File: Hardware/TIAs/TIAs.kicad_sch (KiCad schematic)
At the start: 13 parts, among them U1 MCP6L01x-xOT, U5 MCP6L01x-xOT

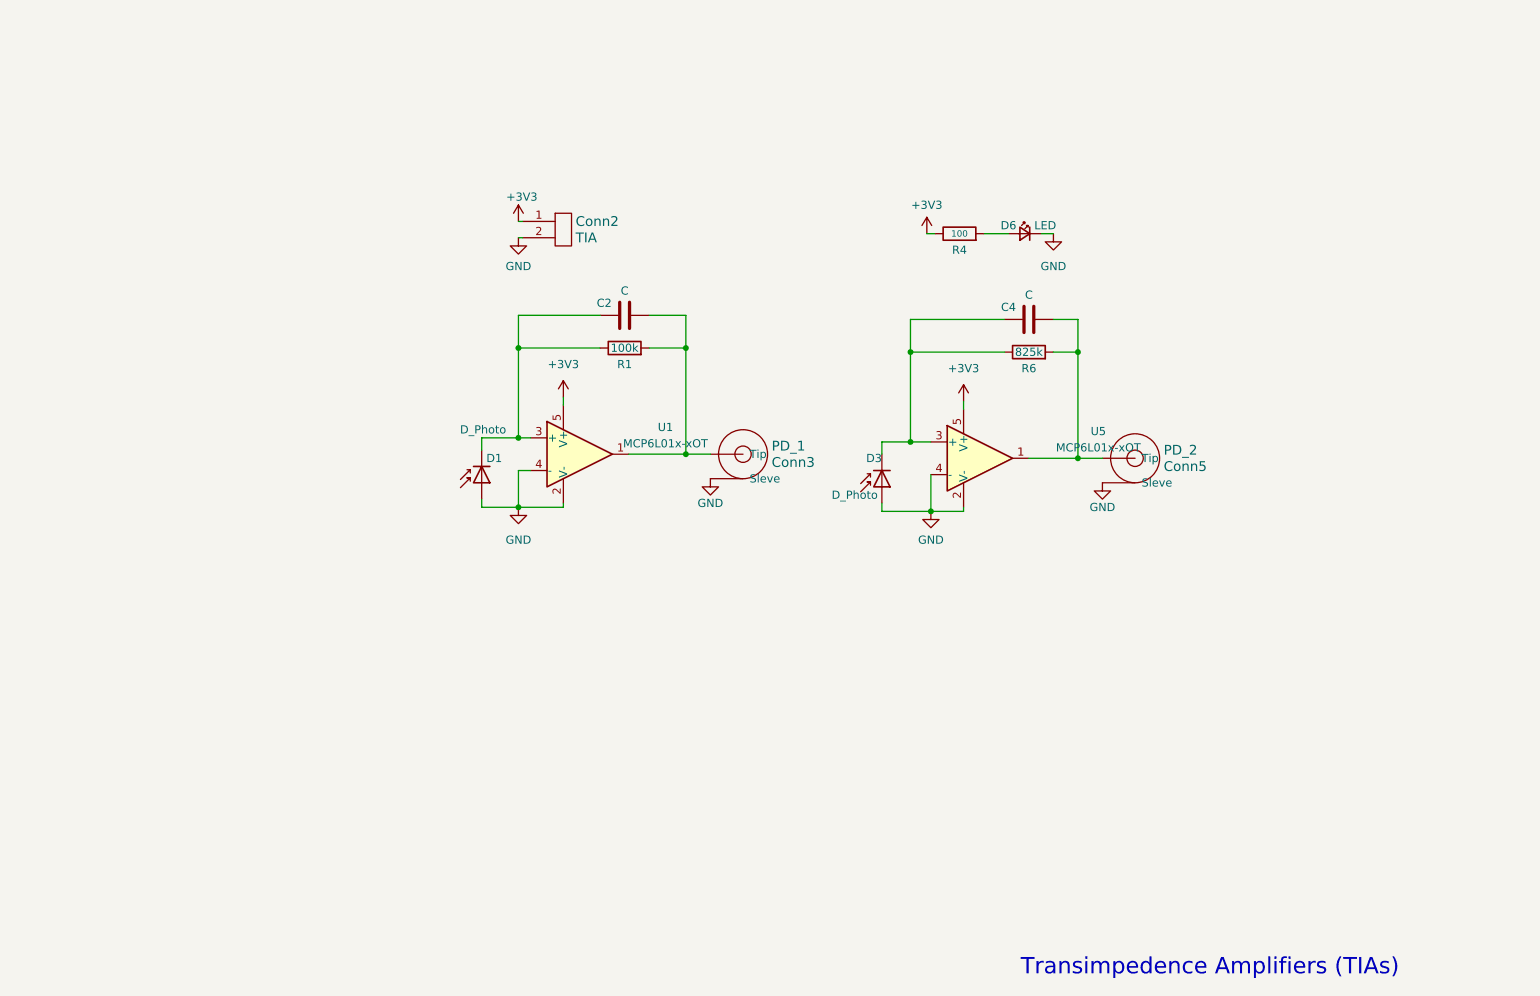
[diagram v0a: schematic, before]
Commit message: Footprint assignments
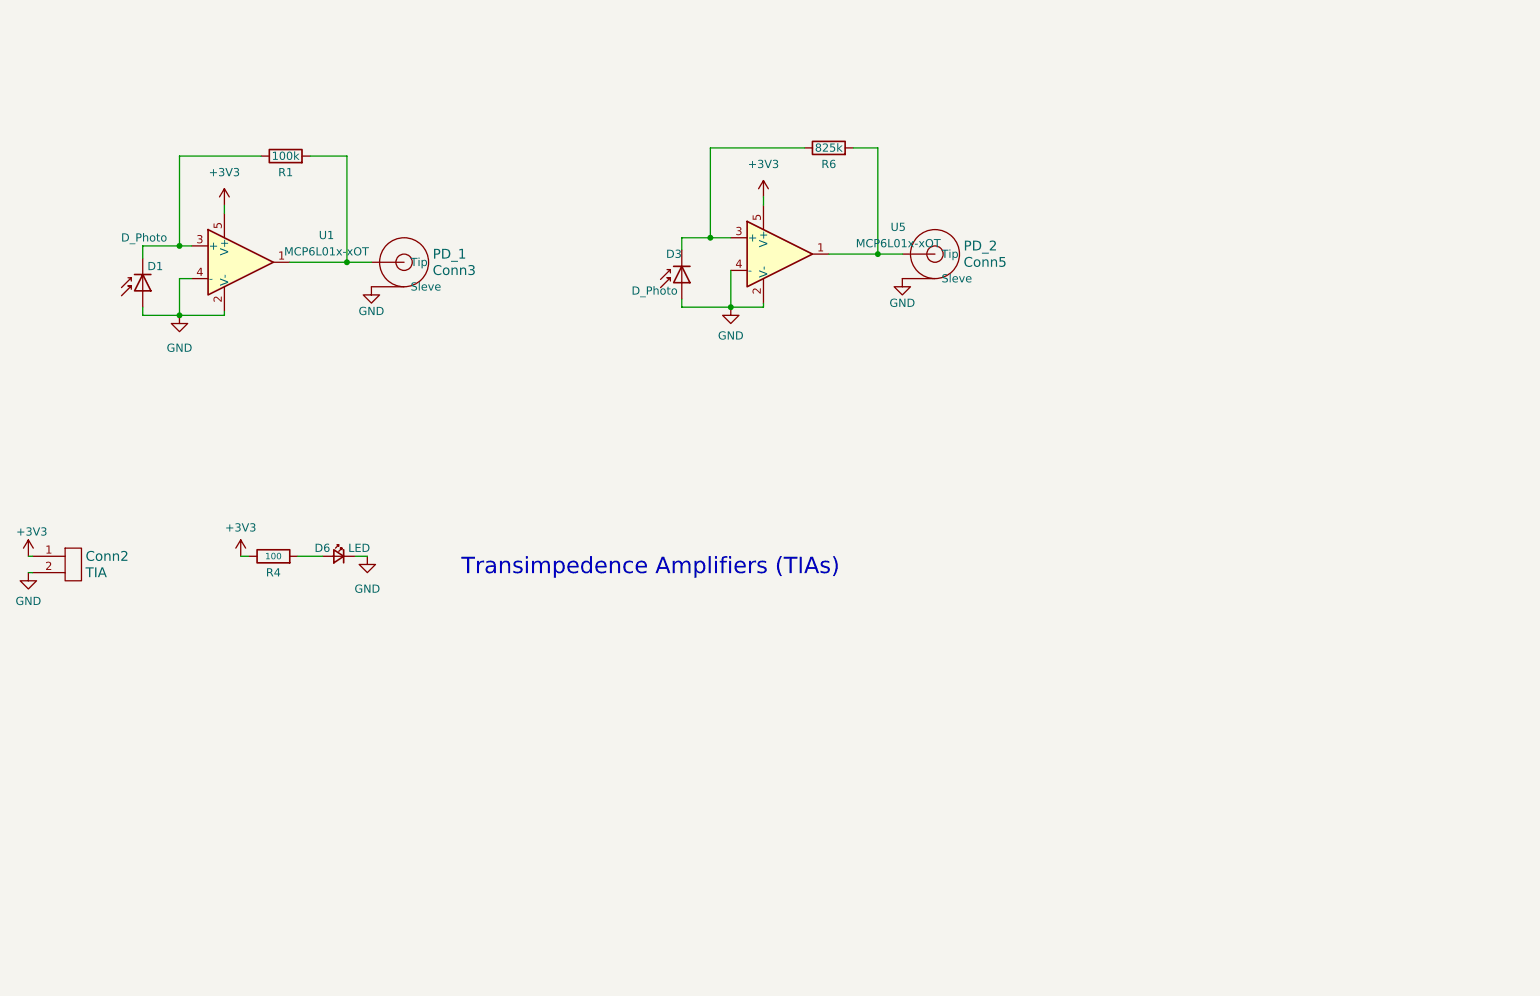
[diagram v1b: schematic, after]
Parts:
- removed C2, C4: C, symbol Device:C
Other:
- moved on the sheet: Conn2, Conn3, Conn5, D1, D3, D6, R1, R4, R6, U1, U5

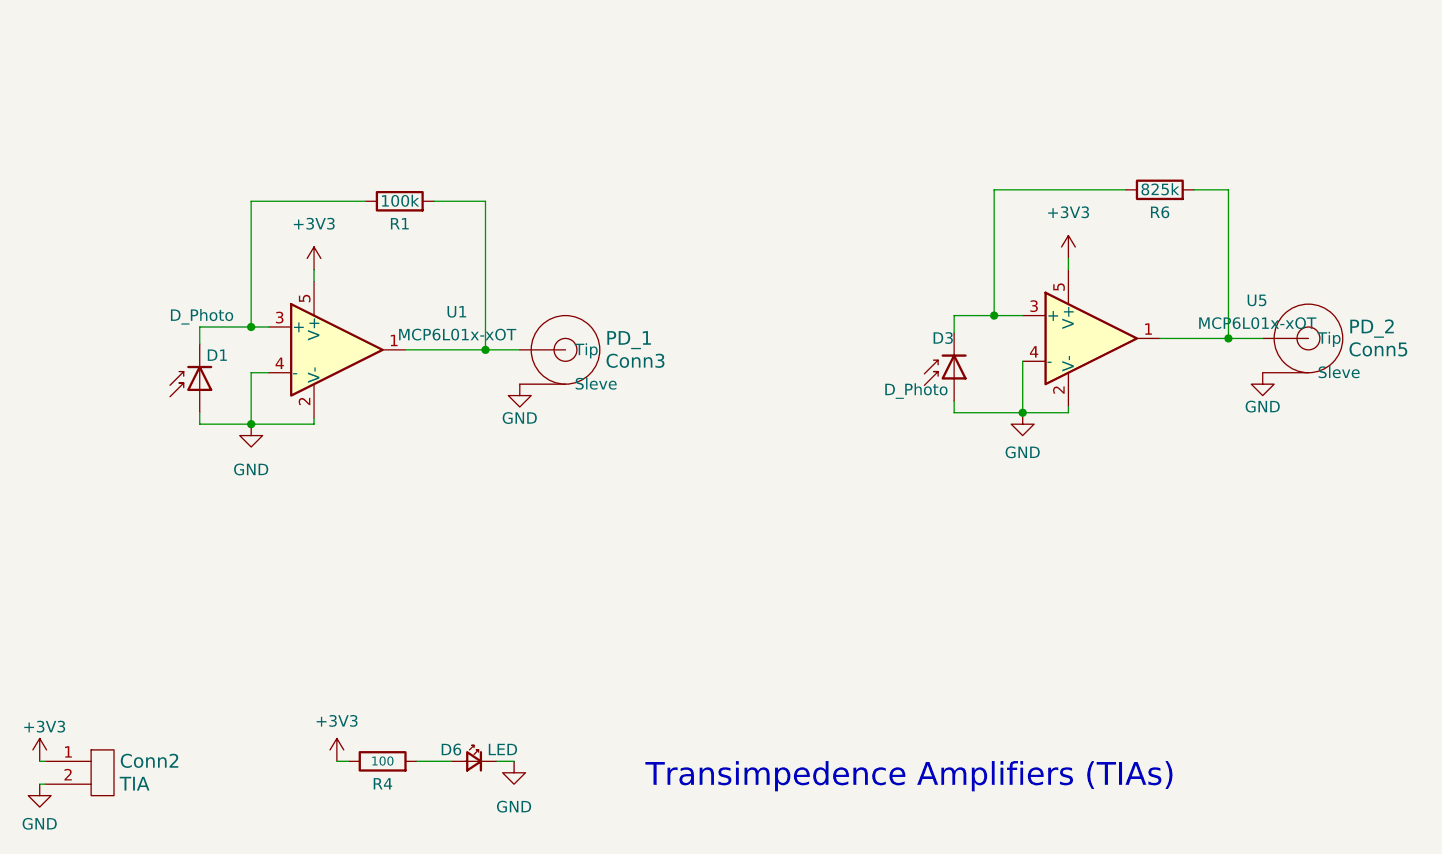
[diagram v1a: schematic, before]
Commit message: Separated Layouts
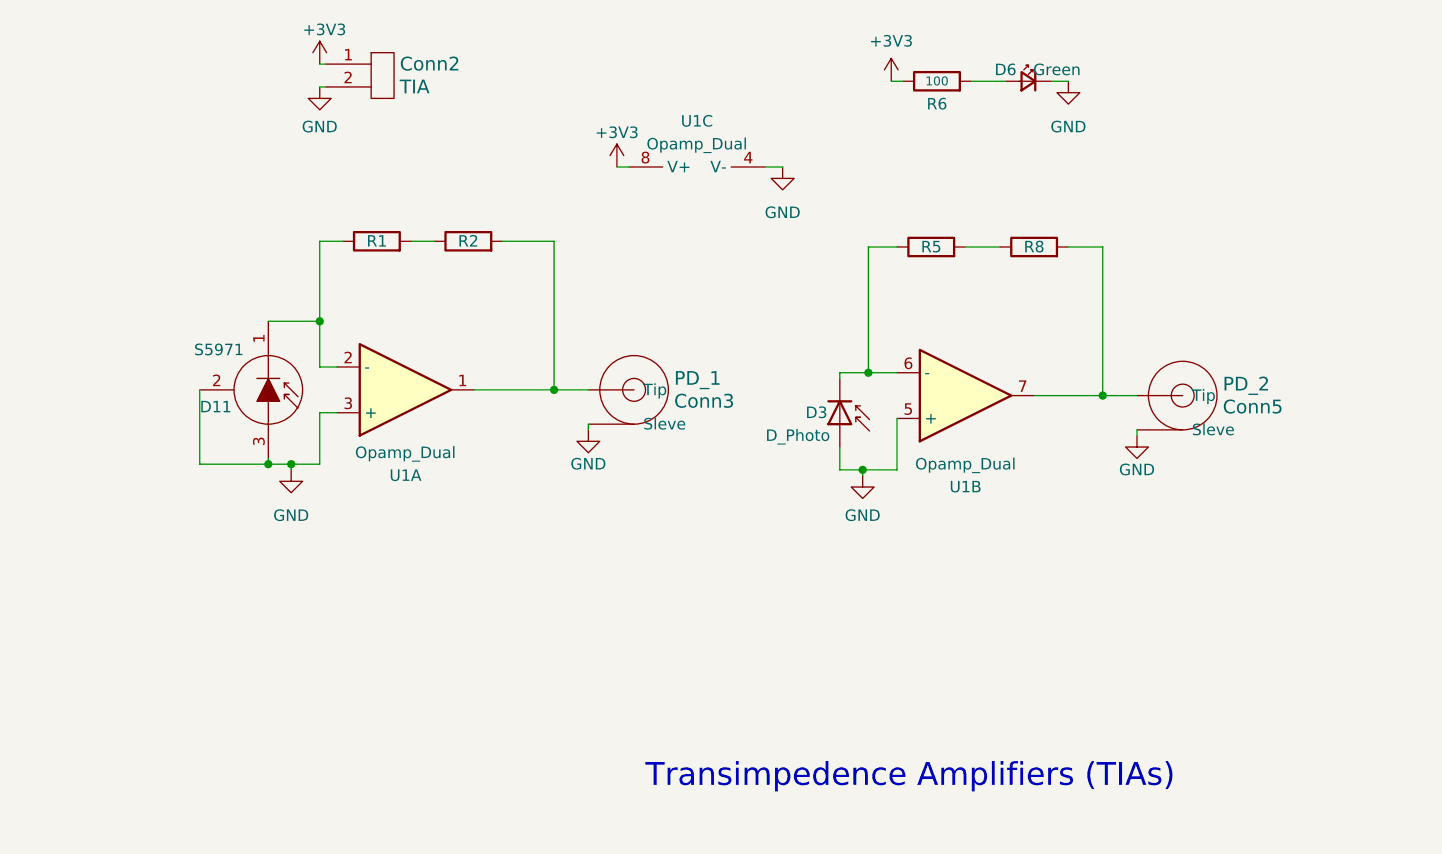
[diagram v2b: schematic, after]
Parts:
- removed D1: D_Photo, symbol Device:D_Photo
- removed R4: 100, Resistor_SMD:R_0603_1608Metric_Pad0.98x0.95mm_HandSolder, symbol Device:R
- removed U1, U5: MCP6L01x-xOT, Package_TO_SOT_SMD:SOT-23-5, symbol Amplifier_Operational:MCP6L01x-xOT
- added D11: S5971, FTIR_Footprints:P16113-011MN, symbol Sensor_Optical:S5971
- added R2, R5, R8: ~, LED_SMD:LED_0603_1608Metric_Pad1.05x0.95mm_HandSolder, symbol Device:R
- added U1: Opamp_Dual, Package_SO:SO-8_3.9x4.9mm_P1.27mm, symbol Device:Opamp_Dual
- Conn2: footprint (none) -> MRDT_Connectors:MOLEX_SL_02_Vertical
- Conn3, Conn5: footprint (none) -> FTIR_Footprints:142-0701-801
- D3: footprint (none) -> FTIR_Footprints:VTP9812FH
- D6: value LED -> Green
- R1: value 100k -> ~; footprint (none) -> LED_SMD:LED_0603_1608Metric_Pad1.05x0.95mm_HandSolder
- R6: value 825k -> 100; footprint (none) -> Resistor_SMD:R_0603_1608Metric_Pad0.98x0.95mm_HandSolder
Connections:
- net +3V3: now also R6.1, U1.8 (V+)
- net GND: now also D11.2 (C), D11.3 (A), U1.3 (+), U1.4 (V-), U1.5 (+)
- net at D3.1 (K): now also R5.1, U1.6 (-); no longer R6.1
- net at R1.1: now also D11.1 (K), U1.2 (-)
- net at Conn3.1 (Tip): now also R2.2, U1.1; no longer R1.2
- net at Conn5.1 (Tip): now also R8.2, U1.7; no longer R6.2
- net at D6.2 (A): now also R6.2
- new net: R1.2, R2.1
- new net: R5.2, R8.1

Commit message: Moved breakout boards to separate layouts
Edge cut no work :,(
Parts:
- added H1, H2, H3, H4: MountingHole, MRDT_Drill_Holes:4_40_Hole_Corner, symbol Mechanical:MountingHole
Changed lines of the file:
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@@
+    )
+  )
+  (symbol (lib_id "Mechanical:MountingHole") (at 160.02 39.37 0) (unit 1)
+    (in_bom yes) (on_board yes) (dnp no) (fields_autoplaced)
+    (property "Reference" "H2" (at 163.195 38.0999 0)
+      (effects (font (size 1.27 1.27)) (justify left))
+    )
+    (property "Value" "MountingHole" (at 163.195 40.6399 0)
+      (effects (font (size 1.27 1.27)) (justify left))
+    )
+    (property "Footprint" "MRDT_Drill_Holes:4_40_Hole_Corner" (at 160.02 39.37 0)
+      (effects (font (size 1.27 1.27)) hide)
+    )
+    (property "Datasheet" "~" (at 160.02 39.37 0)
+      (effects (font (size 1.27 1.27)) hide)
+    )
+    (instances
+      (project "FTIR_Main_Hardware"
+        (path "/049c3f09-c046-40c3-9872-e62b40667976"
+          (reference "H2") (unit 1)
+        )
+      )
+      (project "Flouro_Breakout"
+        (path "/7d297d96-3ae7-4136-8d04-aa7759bb4b4b"
+          (reference "H2") (unit 1)
+        )
+      )
+      (project "TIAs"
+        (path "/9eea0108-5a69-4a2a-bd01-cc036800501a"
+          (reference "H2") (unit 1)
+        )
+      )
     )
   )
@@
         (path "/9eea0108-5a69-4a2a-bd01-cc036800501a"
           (reference "#PWR05") (unit 1)
+        )
+      )
+    )
+  )
+  (symbol (lib_id "Mechanical:MountingHole") (at 160.02 33.02 0) (unit 1)
+    (in_bom yes) (on_board yes) (dnp no) (fields_autoplaced)
+    (property "Reference" "H1" (at 163.195 31.7499 0)
+      (effects (font (size 1.27 1.27)) (justify left))
+    )
+    (property "Value" "MountingHole" (at 163.195 34.2899 0)
+      (effects (font (size 1.27 1.27)) (justify left))
+    )
+    (property "Footprint" "MRDT_Drill_Holes:4_40_Hole_Corner" (at 160.02 33.02 0)
+      (effects (font (size 1.27 1.27)) hide)
+    )
+    (property "Datasheet" "~" (at 160.02 33.02 0)
+      (effects (font (size 1.27 1.27)) hide)
+    )
+    (instances
+      (project "FTIR_Main_Hardware"
+        (path "/049c3f09-c046-40c3-9872-e62b40667976"
+          (reference "H1") (unit 1)
+        )
+      )
+      (project "Flouro_Breakout"
+        (path "/7d297d96-3ae7-4136-8d04-aa7759bb4b4b"
+          (reference "H1") (unit 1)
+        )
+      )
+      (project "TIAs"
+        (path "/9eea0108-5a69-4a2a-bd01-cc036800501a"
+          (reference "H1") (unit 1)
         )
       )
@@
     )
   )
+  (symbol (lib_id "Mechanical:MountingHole") (at 160.02 45.085 0) (unit 1)
+    (in_bom yes) (on_board yes) (dnp no) (fields_autoplaced)
+    (property "Reference" "H3" (at 163.195 43.8149 0)
+      (effects (font (size 1.27 1.27)) (justify left))
+    )
+    (property "Value" "MountingHole" (at 163.195 46.3549 0)
+      (effects (font (size 1.27 1.27)) (justify left))
+    )
+    (property "Footprint" "MRDT_Drill_Holes:4_40_Hole_Corner" (at 160.02 45.085 0)
+      (effects (font (size 1.27 1.27)) hide)
+    )
+    (property "Datasheet" "~" (at 160.02 45.085 0)
+      (effects (font (size 1.27 1.27)) hide)
+    )
+    (instances
+      (project "FTIR_Main_Hardware"
+        (path "/049c3f09-c046-40c3-9872-e62b40667976"
+          (reference "H3") (unit 1)
+        )
+      )
+      (project "Flouro_Breakout"
+        (path "/7d297d96-3ae7-4136-8d04-aa7759bb4b4b"
+          (reference "H3") (unit 1)
+        )
+      )
+      (project "TIAs"
+        (path "/9eea0108-5a69-4a2a-bd01-cc036800501a"
+          (reference "H3") (unit 1)
+        )
+      )
+    )
+  )
   (symbol (lib_id "power:GND") (at 51.435 82.55 0) (unit 1)
     (in_bom yes) (on_board yes) (dnp no) (fields_autoplaced)
@@
         )
       )
+    )
+  )
+  (symbol (lib_id "Mechanical:MountingHole") (at 160.02 50.165 0) (unit 1)
+    (in_bom yes) (on_board yes) (dnp no) (fields_autoplaced)
+    (property "Reference" "H4" (at 163.195 48.8949 0)
+      (effects (font (size 1.27 1.27)) (justify left))
+    )
+    (property "Value" "MountingHole" (at 163.195 51.4349 0)
+      (effects (font (size 1.27 1.27)) (justify left))
+    )
+    (property "Footprint" "MRDT_Drill_Holes:4_40_Hole_Corner" (at 160.02 50.165 0)
+      (effects (font (size 1.27 1.27)) hide)
+    )
+    (property "Datasheet" "~" (at 160.02 50.165 0)
+      (effects (font (size 1.27 1.27)) hide)
+    )
+    (instances
+      (project "FTIR_Main_Hardware"
+        (path "/049c3f09-c046-40c3-9872-e62b40667976"
+          (reference "H4") (unit 1)
+        )
+      )
+      (project "Flouro_Breakout"
+        (path "/7d297d96-3ae7-4136-8d04-aa7759bb4b4b"
+          (reference "H4") (unit 1)
+        )
+      )
+      (project "TIAs"
+        (path "/9eea0108-5a69-4a2a-bd01-cc036800501a"
+          (reference "H4") (unit 1)
+        )
+      )

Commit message: Fixed footprints
Some resistors still had LED footprints which I had thought I had fixed, but failed because I did not also update the schematic.
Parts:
- R1, R2, R5, R8: footprint LED_SMD:LED_0603_1608Metric_Pad1.05x0.95mm_HandSolder -> Resistor_SMD:R_0603_1608Metric_Pad0.98x0.95mm_HandSolder
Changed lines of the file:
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@@
       (effects (font (size 1.27 1.27)))
     )
-    (property "Footprint" "LED_SMD:LED_0603_1608Metric_Pad1.05x0.95mm_HandSolder" (at 71.12 58.928 90)
+    (property "Footprint" "Resistor_SMD:R_0603_1608Metric_Pad0.98x0.95mm_HandSolder" (at 71.12 58.928 90)
       (effects (font (size 1.27 1.27)) hide)
     )
@@
       (effects (font (size 1.27 1.27)))
     )
-    (property "Footprint" "LED_SMD:LED_0603_1608Metric_Pad1.05x0.95mm_HandSolder" (at 60.96 58.928 90)
+    (property "Footprint" "Resistor_SMD:R_0603_1608Metric_Pad0.98x0.95mm_HandSolder" (at 60.96 58.928 90)
       (effects (font (size 1.27 1.27)) hide)
     )
@@
       (effects (font (size 1.27 1.27)))
     )
-    (property "Footprint" "LED_SMD:LED_0603_1608Metric_Pad1.05x0.95mm_HandSolder" (at 122.555 59.563 90)
+    (property "Footprint" "Resistor_SMD:R_0603_1608Metric_Pad0.98x0.95mm_HandSolder" (at 122.555 59.563 90)
       (effects (font (size 1.27 1.27)) hide)
     )
@@
       (effects (font (size 1.27 1.27)))
     )
-    (property "Footprint" "LED_SMD:LED_0603_1608Metric_Pad1.05x0.95mm_HandSolder" (at 133.985 59.563 90)
-      (effects (font (size 1.27 1.27)) hide)
-    )
+    (property "Footprint" "Resistor_SMD:R_0603_1608Metric_Pad0.98x0.95mm_HandSolder" (at 133.985 59.563 90)
+      (effects (font (size 1.27 1.27)) hide)
+    )
